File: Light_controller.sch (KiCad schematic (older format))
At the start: 9 parts, among them U1 LM358DR, U2 PT8211-S, U3 STM8S003K3T

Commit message: added extra circuit for the current sensor
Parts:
- removed U3: STM8S003K3T, Package_QFP:LQFP-32_7x7mm_P0.8mm, symbol MCU_ST_STM8:STM8S003K3T
- added C4: C, symbol Device:C
- added C?: C, Capacitor_SMD:C_0805_2012Metric, symbol Device:C
- added R4, R? (x2): R, Capacitor_SMD:C_0603_1608Metric, symbol Device:R
- added R?: 0.01Ω, Capacitor_SMD:C_0603_1608Metric, symbol Device:R
- added SW1: SW_SPST, symbol Switch:SW_SPST
- added unit 2 of U1
- added U3: STM8S003F3P, Package_SO:TSSOP-20_4.4x6.5mm_P0.65mm, symbol MCU_ST_STM8:STM8S003F3P
- added U4, U5: LTV-356T, digikey-footprints:SMD-4_4.4x3.85mm_P2.54mm, symbol dk_Optoisolators-Transistor-Photovoltaic-Output:LTV-356T
- added U6: TLV1117-50, symbol Regulator_Linear:TLV1117-50
- C1, C2, C3: footprint (none) -> Capacitor_SMD:C_0805_2012Metric
- R1, R2, R3: footprint (none) -> Capacitor_SMD:C_0603_1608Metric
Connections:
- net labels added: +12V, 5V_SUPPLY, CURRENT_IN, C_SENSOR, PA1, PA2, PA3, PB5, PC4, PC7, PD2, RCH, RESET, RX_in, SPI_MOSI, SPI_SCK, SWIM, TX_in, UART_CLOCK, UART_RX, UART_TX, VCAP, VSS, V_SENSOR, WS
- net labels removed: OUt, VDD
- wire segments 41 -> 80
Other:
- note added: "Current Sensor"
- note added: "DAC Amplifier"
- note added: "External DAC"
- note added: "From STM32\n"
- note added: "Low drop-out regulator"
- note added: "Microcontroller STM8"
- note added: "Output signal 0 to 10V\nto the power supply\n for LED intensity\n\n"
- note added: "Reset Circuit"
- note added: "This LCH \nwill drill a hole \nor something for extra function\n"
- note added: "gain 100 to 600"
- note added: "gain is 3x\n"
- note added: "reserved for sensor\n"
- moved on the sheet: C1, C2, C3, R1, R2, R3, U2

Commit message: added all circuit except temperature sensor
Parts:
- removed SW1: SW_SPST, symbol Switch:SW_SPST
- removed U1: LM358DR, digikey-footprints:SOIC-8_W3.9mm, symbol dk_Linear-Amplifiers-Instrumentation-OP-Amps-Buffer-Amps:LM358DR
- removed U4, U5: LTV-356T, digikey-footprints:SMD-4_4.4x3.85mm_P2.54mm, symbol dk_Optoisolators-Transistor-Photovoltaic-Output:LTV-356T
- removed U6: TLV1117-50, symbol Regulator_Linear:TLV1117-50
- added C6: C, Capacitor_SMD:C_0805_2012Metric, symbol Device:C
- added C7: 470uF, Capacitor_SMD:CP_Elec_6.3x7.7, symbol Device:C
- added D1: 1N5819HW, Diode_SMD:D_SOD-123, symbol Diode:1N5819
- added R10, R8, R9: R, Resistor_SMD:R_0603_1608Metric, symbol Device:R
- added R11: 1K, Resistor_SMD:R_0603_1608Metric, symbol Device:R
- added U1: LM358, Package_SO:SOIC-8_3.9x4.9mm_P1.27mm, symbol Amplifier_Operational:LM358
- added U10, U11, U9: PH2.0_horizontal, Connector_JST:JST_PH_S2B-PH-K_1x02_P2.00mm_Horizontal, symbol Custom_Library:PH2.0_horizontal
- added U4: SMD_2062, Custom_footprint_lib:LEDSMD2062, symbol Custom_Library:SMD_2062
- added U5: tact_sw, Button_Switch_SMD:SW_SPST_SKQG_WithStem, symbol Custom_Library:tact_sw
- added U6: AMS1117-5.0, Package_TO_SOT_SMD:SOT-223, symbol Regulator_Linear:AMS1117-5.0
- added U7, U8: EL357N-C, Package_SO:SOP-4_3.8x4.1mm_P2.54mm, symbol Custom_Library:EL357N-C
- C4: footprint (none) -> Capacitor_SMD:C_0805_2012Metric
- R1, R2, R3, R4: footprint Capacitor_SMD:C_0603_1608Metric -> Resistor_SMD:R_0603_1608Metric
- R5, R6, R7: renamed from R?; footprint Capacitor_SMD:C_0603_1608Metric -> Resistor_SMD:R_0603_1608Metric
- gave numbers to parts that had none: 1
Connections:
- net labels added: 12V_INPUT, 5V_EXT, EXT_GND, Tx_Rx
- net labels removed: +12V, VSS
- wire segments 80 -> 104
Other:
- note added: "Connection to STM32"
- note added: "Different Power Domain"
- note added: "External 5V"
- note added: "LDO 5V"
- note added: "opto_isolator for UART"
- moved on the sheet: C1, C2, R2

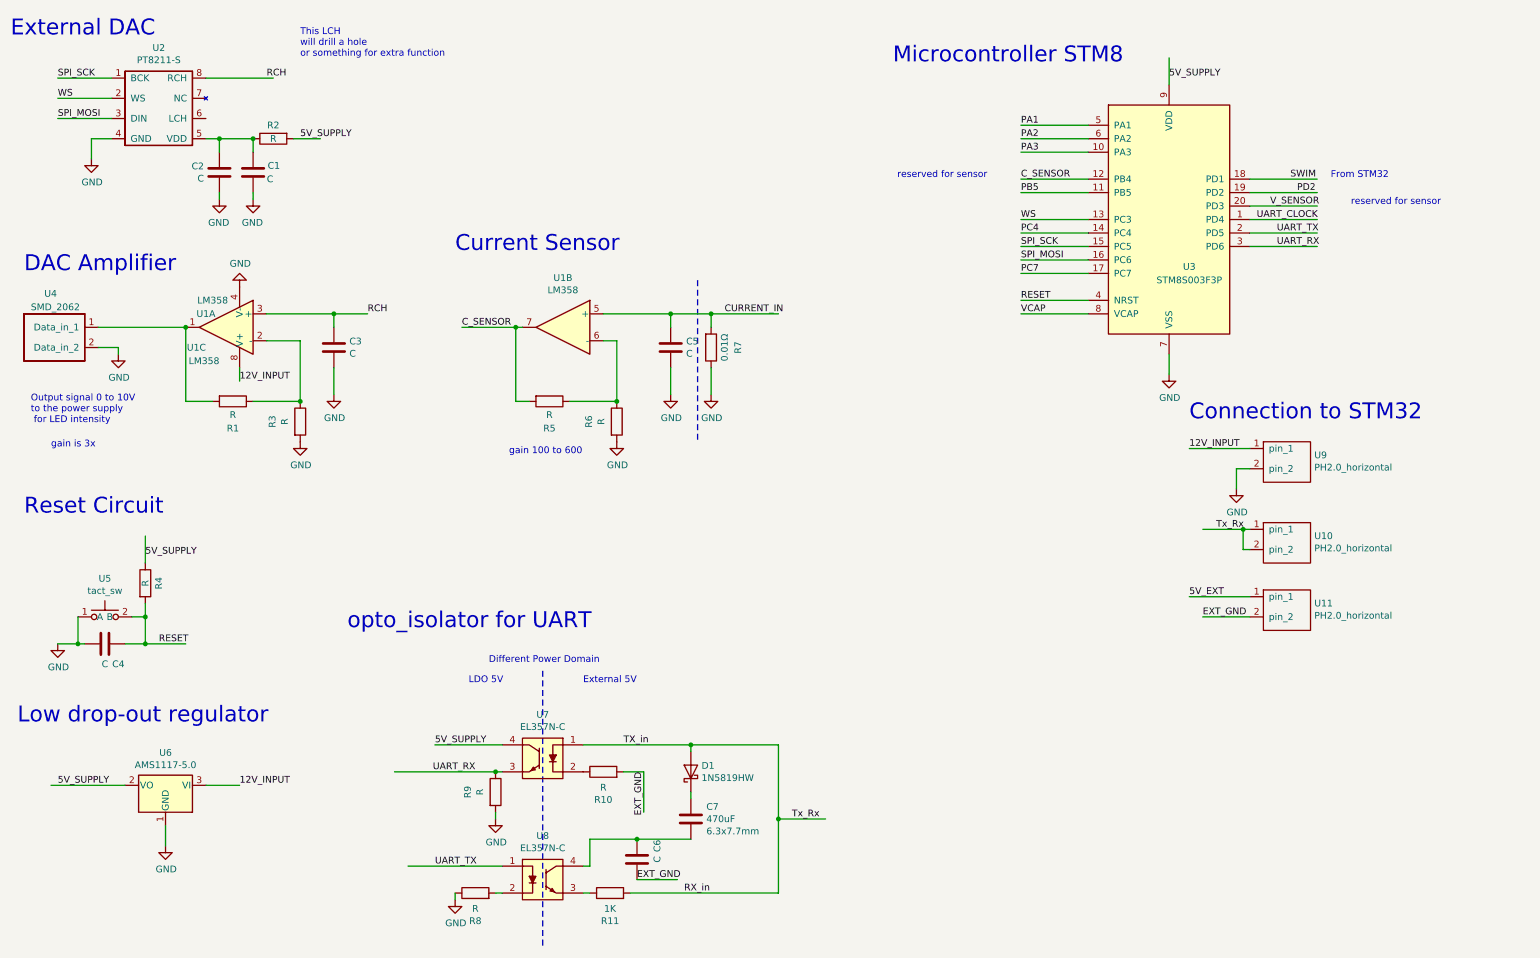
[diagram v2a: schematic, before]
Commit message: modified ph2.0 to smd , changed thermistor to a ph2.0 and rerouted the layout again with via
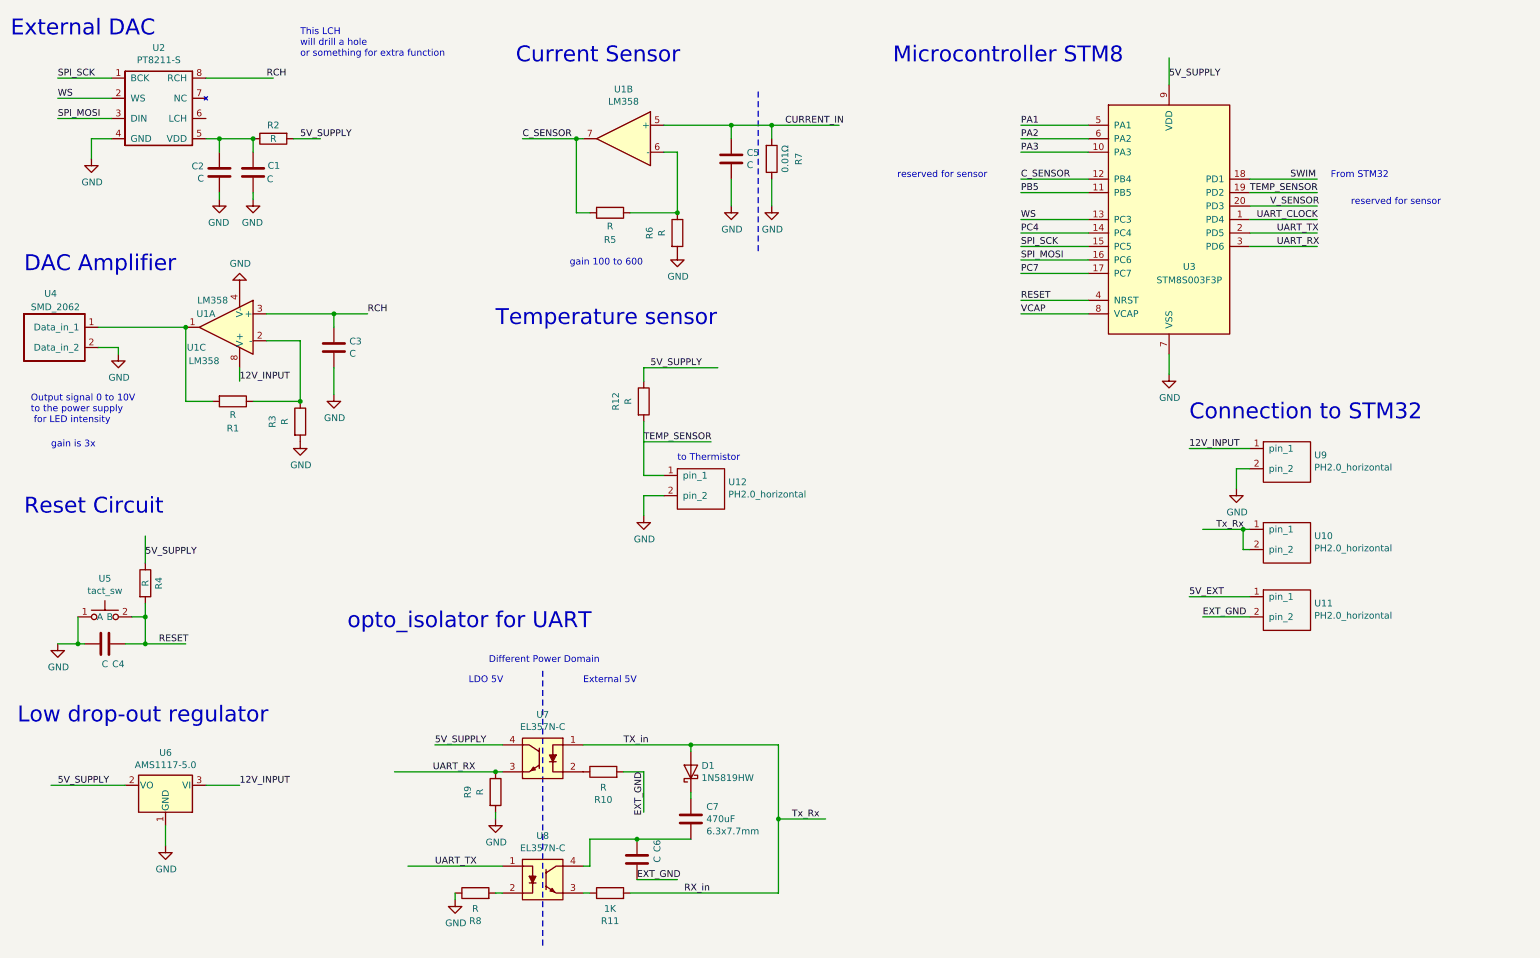
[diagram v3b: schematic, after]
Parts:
- added R12: R, Resistor_SMD:R_0603_1608Metric, symbol Device:R
- added U12: PH2.0_horizontal, Connector_JST:JST_PH_S2B-PH-SM4-TB_1x02-1MP_P2.00mm_Horizontal, symbol Custom_Library:PH2.0_horizontal
- U10, U11, U9: footprint Connector_JST:JST_PH_S2B-PH-K_1x02_P2.00mm_Horizontal -> Connector_JST:JST_PH_S2B-PH-SM4-TB_1x02-1MP_P2.00mm_Horizontal
- U6: footprint Package_TO_SOT_SMD:SOT-223 -> Package_TO_SOT_SMD:SOT-223-3_TabPin2
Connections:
- net labels added: TEMP_SENSOR
- net labels removed: PD2
- wire segments 104 -> 111
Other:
- note added: "Temperature sensor"
- note added: "to Thermistor"
- moved on the sheet: C5, R5, R6, R7, U1B
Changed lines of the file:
@@
 Text Label 7950 2700 0    50   ~ 0
 VCAP
-Text Label 10000 1800 0    50   ~ 0
-PD2
+Text Label 9650 1800 0    50   ~ 0
+TEMP_SENSOR
 Text Label 9800 1900 0    50   ~ 0
 V_SENSOR
@@
 L Device:R R5
 U 1 1 5E77157A
-P 4450 3350
-F 0 "R5" V 4650 3350 50  0000 C CNN
-F 1 "R" V 4550 3350 50  0000 C CNN
-F 2 "Resistor_SMD:R_0603_1608Metric" V 4380 3350 50  0001 C CNN
-F 3 "~" H 4450 3350 50  0001 C CNN
-	1    4450 3350
+P 4900 1950
+F 0 "R5" V 5100 1950 50  0000 C CNN
+F 1 "R" V 5000 1950 50  0000 C CNN
+F 2 "Resistor_SMD:R_0603_1608Metric" V 4830 1950 50  0001 C CNN
+F 3 "~" H 4900 1950 50  0001 C CNN
+	1    4900 1950
 	0    1    1    0
 $EndComp
 Wire Wire Line
-	4600 3350 4950 3350
-Wire Wire Line
-	4950 2900 4950 3350
+	5050 1950 5400 1950
+Wire Wire Line
+	5400 1500 5400 1950
 $Comp
 L power:GND #PWR0107
 U 1 1 5E771584
-P 4950 3650
-F 0 "#PWR0107" H 4950 3400 50  0001 C CNN
-F 1 "GND" H 4955 3477 50  0000 C CNN
-F 2 "" H 4950 3650 50  0001 C CNN
-F 3 "" H 4950 3650 50  0001 C CNN
-	1    4950 3650
+P 5400 2250
+F 0 "#PWR0107" H 5400 2000 50  0001 C CNN
+F 1 "GND" H 5405 2077 50  0000 C CNN
+F 2 "" H 5400 2250 50  0001 C CNN
+F 3 "" H 5400 2250 50  0001 C CNN
+	1    5400 2250
 	1    0    0    -1
 $EndComp
@@
 L Device:R R6
 U 1 1 5E77158A
-P 4950 3500
-F 0 "R6" V 4743 3500 50  0000 C CNN
-F 1 "R" V 4834 3500 50  0000 C CNN
-F 2 "Resistor_SMD:R_0603_1608Metric" V 4880 3500 50  0001 C CNN
-F 3 "~" H 4950 3500 50  0001 C CNN
-	1    4950 3500
-	1    0    0    -1
-$EndComp
-Connection ~ 4950 3350
-Wire Wire Line
-	4950 2900 4850 2900
+P 5400 2100
+F 0 "R6" V 5193 2100 50  0000 C CNN
+F 1 "R" V 5284 2100 50  0000 C CNN
+F 2 "Resistor_SMD:R_0603_1608Metric" V 5330 2100 50  0001 C CNN
+F 3 "~" H 5400 2100 50  0001 C CNN
+	1    5400 2100
+	1    0    0    -1
+$EndComp
+Connection ~ 5400 1950
+Wire Wire Line
+	5400 1500 5300 1500
 $Comp
 L Device:C C5
 U 1 1 5E77749C
-P 5350 2950
-F 0 "C5" H 5465 2996 50  0000 L CNN
-F 1 "C" H 5465 2905 50  0000 L CNN
-F 2 "Capacitor_SMD:C_0805_2012Metric" H 5388 2800 50  0001 C CNN
-F 3 "~" H 5350 2950 50  0001 C CNN
-	1    5350 2950
-	1    0    0    -1
-$EndComp
-Wire Wire Line
-	5350 3300 5350 3100
+P 5800 1550
+F 0 "C5" H 5915 1596 50  0000 L CNN
+F 1 "C" H 5915 1505 50  0000 L CNN
+F 2 "Capacitor_SMD:C_0805_2012Metric" H 5838 1400 50  0001 C CNN
+F 3 "~" H 5800 1550 50  0001 C CNN
+	1    5800 1550
+	1    0    0    -1
+$EndComp
+Wire Wire Line
+	5800 1900 5800 1700
 $Comp
 L power:GND #PWR0108
 U 1 1 5E7774A3
-P 5350 3300
-F 0 "#PWR0108" H 5350 3050 50  0001 C CNN
-F 1 "GND" H 5355 3127 50  0000 C CNN
-F 2 "" H 5350 3300 50  0001 C CNN
-F 3 "" H 5350 3300 50  0001 C CNN
-	1    5350 3300
-	1    0    0    -1
-$EndComp
-Wire Wire Line
-	5350 2800 5350 2700
-Wire Wire Line
-	4850 2700 5350 2700
-Text Label 3800 2800 0    50   ~ 0
+P 5800 1900
+F 0 "#PWR0108" H 5800 1650 50  0001 C CNN
+F 1 "GND" H 5805 1727 50  0000 C CNN
+F 2 "" H 5800 1900 50  0001 C CNN
+F 3 "" H 5800 1900 50  0001 C CNN
+	1    5800 1900
+	1    0    0    -1
+$EndComp
+Wire Wire Line
+	5800 1400 5800 1300
+Wire Wire Line
+	5300 1300 5800 1300
+Text Label 4250 1400 0    50   ~ 0
 C_SENSOR
 Wire Wire Line
-	3800 2800 4200 2800
-Wire Wire Line
-	4300 3350 4200 3350
-Wire Wire Line
-	4200 3350 4200 2800
-Connection ~ 4200 2800
-Wire Wire Line
-	4200 2800 4250 2800
-Text Notes 4150 3750 0    50   ~ 0
+	4250 1400 4650 1400
+Wire Wire Line
+	4750 1950 4650 1950
+Wire Wire Line
+	4650 1950 4650 1400
+Connection ~ 4650 1400
+Wire Wire Line
+	4650 1400 4700 1400
+Text Notes 4600 2350 0    50   ~ 0
 gain 100 to 600
 Wire Wire Line
-	5650 2800 5650 2700
-Wire Wire Line
-	5650 2700 5350 2700
-Connection ~ 5350 2700
-Wire Wire Line
-	5650 3300 5650 3100
+	6100 1400 6100 1300
+Wire Wire Line
+	6100 1300 5800 1300
+Connection ~ 5800 1300
+Wire Wire Line
+	6100 1900 6100 1700
 $Comp
 L power:GND #PWR0109
 U 1 1 5E7B6689
-P 5650 3300
-F 0 "#PWR0109" H 5650 3050 50  0001 C CNN
-F 1 "GND" H 5655 3127 50  0000 C CNN
-F 2 "" H 5650 3300 50  0001 C CNN
-F 3 "" H 5650 3300 50  0001 C CNN
-	1    5650 3300
-	1    0    0    -1
-$EndComp
-Wire Wire Line
-	5650 2700 6150 2700
-Connection ~ 5650 2700
-Text Label 5750 2700 0    50   ~ 0
+P 6100 1900
+F 0 "#PWR0109" H 6100 1650 50  0001 C CNN
+F 1 "GND" H 6105 1727 50  0000 C CNN
+F 2 "" H 6100 1900 50  0001 C CNN
+F 3 "" H 6100 1900 50  0001 C CNN
+	1    6100 1900
+	1    0    0    -1
+$EndComp
+Wire Wire Line
+	6100 1300 6600 1300
+Connection ~ 6100 1300
+Text Label 6200 1300 0    50   ~ 0
 CURRENT_IN
 $Comp
 L Device:R R7
 U 1 1 5E7AC3E6
-P 5650 2950
-F 0 "R7" V 5850 2950 50  0000 C CNN
-F 1 "0.01Ω" V 5750 2950 50  0000 C CNN
-F 2 "Resistor_SMD:R_0603_1608Metric" V 5580 2950 50  0001 C CNN
-F 3 "~" H 5650 2950 50  0001 C CNN
-	1    5650 2950
+P 6100 1550
+F 0 "R7" V 6300 1550 50  0000 C CNN
+F 1 "0.01Ω" V 6200 1550 50  0000 C CNN
+F 2 "Resistor_SMD:R_0603_1608Metric" V 6030 1550 50  0001 C CNN
+F 3 "~" H 6100 1550 50  0001 C CNN
+	1    6100 1550
 	1    0    0    1
 $EndComp
 Wire Notes Line
-	5550 2450 5550 3650
+	6000 1050 6000 2250
 Wire Wire Line
 	2250 1800 2250 1850
@@
 	1    0    0    1
 $EndComp
-Text Notes 3750 2250 0    118  ~ 0
+Text Notes 4200 850  0    118  ~ 0
 Current Sensor
-$Comp
-L Amplifier_Operational:LM358 U1
-U 2 1 5E6B73DD
-P 4550 2800
-F 0 "U1" H 4550 3167 50  0000 C CNN
-F 1 "LM358" H 4550 3076 50  0000 C CNN
-F 2 "Package_SO:SOIC-8_3.9x4.9mm_P1.27mm" H 4550 2800 50  0001 C CNN
-F 3 "http://www.ti.com/lit/ds/symlink/lm2904-n.pdf" H 4550 2800 50  0001 C CNN
-	2    4550 2800
-	-1   0    0    -1
-$EndComp
 $Comp
 L Amplifier_Operational:LM358 U1
@@
 Text Notes 4700 5450 0    50   ~ 0
 External 5V
-$Comp
-L Regulator_Linear:AMS1117-5.0 U6
-U 1 1 5E70587E
-P 1600 6200
-F 0 "U6" H 1600 6442 50  0000 C CNN
-F 1 "AMS1117-5.0" H 1600 6351 50  0000 C CNN
-F 2 "Package_TO_SOT_SMD:SOT-223" H 1600 6400 50  0001 C CNN
-F 3 "http://www.advanced-monolithic.com/pdf/ds1117.pdf" H 1700 5950 50  0001 C CNN
-	1    1600 6200
-	-1   0    0    -1
-$EndComp
 Wire Wire Line
 	4050 6400 4050 6450
@@
 F 0 "U10" H 10128 4051 50  0000 L CNN
 F 1 "PH2.0_horizontal" H 10128 3960 50  0000 L CNN
-F 2 "Connector_JST:JST_PH_S2B-PH-K_1x02_P2.00mm_Horizontal" H 9900 4200 50  0001 C CNN
+F 2 "Connector_JST:JST_PH_S2B-PH-SM4-TB_1x02-1MP_P2.00mm_Horizontal" H 9900 4200 50  0001 C CNN
 F 3 "" H 9900 4200 50  0001 C CNN
 	1    9900 4200
@@
 F 0 "U11" H 10128 4551 50  0000 L CNN
 F 1 "PH2.0_horizontal" H 10128 4460 50  0000 L CNN
-F 2 "Connector_JST:JST_PH_S2B-PH-K_1x02_P2.00mm_Horizontal" H 9900 4700 50  0001 C CNN
+F 2 "Connector_JST:JST_PH_S2B-PH-SM4-TB_1x02-1MP_P2.00mm_Horizontal" H 9900 4700 50  0001 C CNN
 F 3 "" H 9900 4700 50  0001 C CNN
 	1    9900 4700
@@
 Text Notes 9200 3500 0    118  ~ 0
 Connection to STM32
-$Comp
-L Custom_Library:PH2.0_horizontal U9
-U 1 1 5E74D8D5
-P 9900 3600
-F 0 "U9" H 10128 3451 50  0000 L CNN
-F 1 "PH2.0_horizontal" H 10128 3360 50  0000 L CNN
-F 2 "Connector_JST:JST_PH_S2B-PH-K_1x02_P2.00mm_Horizontal" H 9900 3600 50  0001 C CNN
-F 3 "" H 9900 3600 50  0001 C CNN
-	1    9900 3600
-	1    0    0    -1
-$EndComp
 Text Notes 450  650  0    118  ~ 0
 External DAC
@@
 	9550 3850 9550 4000
 $Comp
-L power:GND #PWR?
+L power:GND #PWR02
 U 1 1 5E76470F
 P 9550 4000
-F 0 "#PWR?" H 9550 3750 50  0001 C CNN
+F 0 "#PWR02" H 9550 3750 50  0001 C CNN
 F 1 "GND" H 9555 3827 50  0000 C CNN
 F 2 "" H 9550 4000 50  0001 C CNN
@@
 Text Label 2150 3200 0    50   ~ 0
 12V_INPUT
+Text Notes 4050 2800 0    118  ~ 0
+Temperature sensor
+Wire Wire Line
+	5700 3100 5150 3100
+Text Label 5200 3100 0    50   ~ 0
+5V_SUPPLY
+$Comp
+L Device:R R12
+U 1 1 5E778979
+P 5150 3350
+F 0 "R12" V 4943 3350 50  0000 C CNN
+F 1 "R" V 5034 3350 50  0000 C CNN
+F 2 "Resistor_SMD:R_0603_1608Metric" V 5080 3350 50  0001 C CNN
+F 3 "~" H 5150 3350 50  0001 C CNN
+	1    5150 3350
+	1    0    0    -1
+$EndComp
+Wire Wire Line
+	5150 3100 5150 3200
+$Comp
+L power:GND #PWR01
+U 1 1 5E784F52
+P 5150 4200
+F 0 "#PWR01" H 5150 3950 50  0001 C CNN
+F 1 "GND" H 5155 4027 50  0000 C CNN
+F 2 "" H 5150 4200 50  0001 C CNN
+F 3 "" H 5150 4200 50  0001 C CNN
+	1    5150 4200
+	1    0    0    -1
+$EndComp
+Wire Wire Line
+	5150 3650 5650 3650
+Text Label 5150 3650 0    50   ~ 0
+TEMP_SENSOR
+$Comp
+L Amplifier_Operational:LM358 U1
+U 2 1 5E6B73DD
+P 5000 1400
+F 0 "U1" H 5000 1767 50  0000 C CNN
+F 1 "LM358" H 5000 1676 50  0000 C CNN
+F 2 "Package_SO:SOIC-8_3.9x4.9mm_P1.27mm" H 5000 1400 50  0001 C CNN
+F 3 "http://www.ti.com/lit/ds/symlink/lm2904-n.pdf" H 5000 1400 50  0001 C CNN
+	2    5000 1400
+	-1   0    0    -1
+$EndComp
+$Comp
+L Custom_Library:PH2.0_horizontal U9
+U 1 1 5E74D8D5
+P 9900 3600
+F 0 "U9" H 10128 3451 50  0000 L CNN
+F 1 "PH2.0_horizontal" H 10128 3360 50  0000 L CNN
+F 2 "Connector_JST:JST_PH_S2B-PH-SM4-TB_1x02-1MP_P2.00mm_Horizontal" H 9900 3600 50  0001 C CNN
+F 3 "" H 9900 3600 50  0001 C CNN
+	1    9900 3600
+	1    0    0    -1
+$EndComp
+$Comp
+L Custom_Library:PH2.0_horizontal U12
+U 1 1 5E79BBBF
+P 5550 3800
+F 0 "U12" H 5778 3651 50  0000 L CNN
+F 1 "PH2.0_horizontal" H 5778 3560 50  0000 L CNN
+F 2 "Connector_JST:JST_PH_S2B-PH-SM4-TB_1x02-1MP_P2.00mm_Horizontal" H 5550 3800 50  0001 C CNN
+F 3 "" H 5550 3800 50  0001 C CNN
+	1    5550 3800
+	1    0    0    -1
+$EndComp
+Wire Wire Line
+	5150 3900 5300 3900
+Wire Wire Line
+	5150 3500 5150 3900
+Wire Wire Line
+	5300 4050 5150 4050
+Wire Wire Line
+	5150 4050 5150 4200
+Text Notes 5400 3800 0    50   ~ 0
+to Thermistor
+$Comp
+L Regulator_Linear:AMS1117-5.0 U6
+U 1 1 5E7C43A9
+P 1600 6200
+F 0 "U6" H 1600 6442 50  0000 C CNN
+F 1 "AMS1117-5.0" H 1600 6351 50  0000 C CNN
+F 2 "Package_TO_SOT_SMD:SOT-223-3_TabPin2" H 1600 6400 50  0001 C CNN
+F 3 "http://www.advanced-monolithic.com/pdf/ds1117.pdf" H 1700 5950 50  0001 C CNN
+	1    1600 6200
+	-1   0    0    -1
+$EndComp
 $EndSCHEMATC

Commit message: updated newer schematic , havent add the custom footprint and havent change the design layout
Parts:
- added C? (x3): C, Capacitor_SMD:C_0805_2012Metric, symbol Device:C
- added D? (x2): D_Zener, symbol Device:D_Zener
- added JP?: SolderJumper_2_Open, symbol Jumper:SolderJumper_2_Open
- added R? (x2): R, Resistor_SMD:R_0603_1608Metric, symbol Device:R
- added U?: SMD2063, symbol Custom_Library:SMD2063
- added U?: PinSocket_1x4, symbol Custom_Library:PinSocket_1x4
- R7: footprint Resistor_SMD:R_0603_1608Metric -> Resistor_SMD:R_1210_3225Metric
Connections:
- net labels added: LED+, LED-, LED_SENSE
- net labels removed: CURRENT_IN
- wire segments 111 -> 136
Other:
- note added: "(0 to 5V)\n"
- note added: "Voltage Sensor"
- note added: "Voltage and current for sensor"
- note added: "max 80V"
- note removed: "From STM32\n"
- note removed: "reserved for sensor\n"
- moved on the sheet: R12, U10, U11, U12, U3, U9
